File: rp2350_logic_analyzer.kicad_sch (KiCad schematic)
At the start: 35 parts, among them J1 Conn_02x04, J2 Conn_01x03, J3 Conn_01x03, J4 Conn_01x03, J5 Conn_01x03, U2 TLV3501AIDBV, U3 TLV3501AIDBV, U4 TLV3501AIDBV, U5 TLV3501AIDBV, U6 SRV05-4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

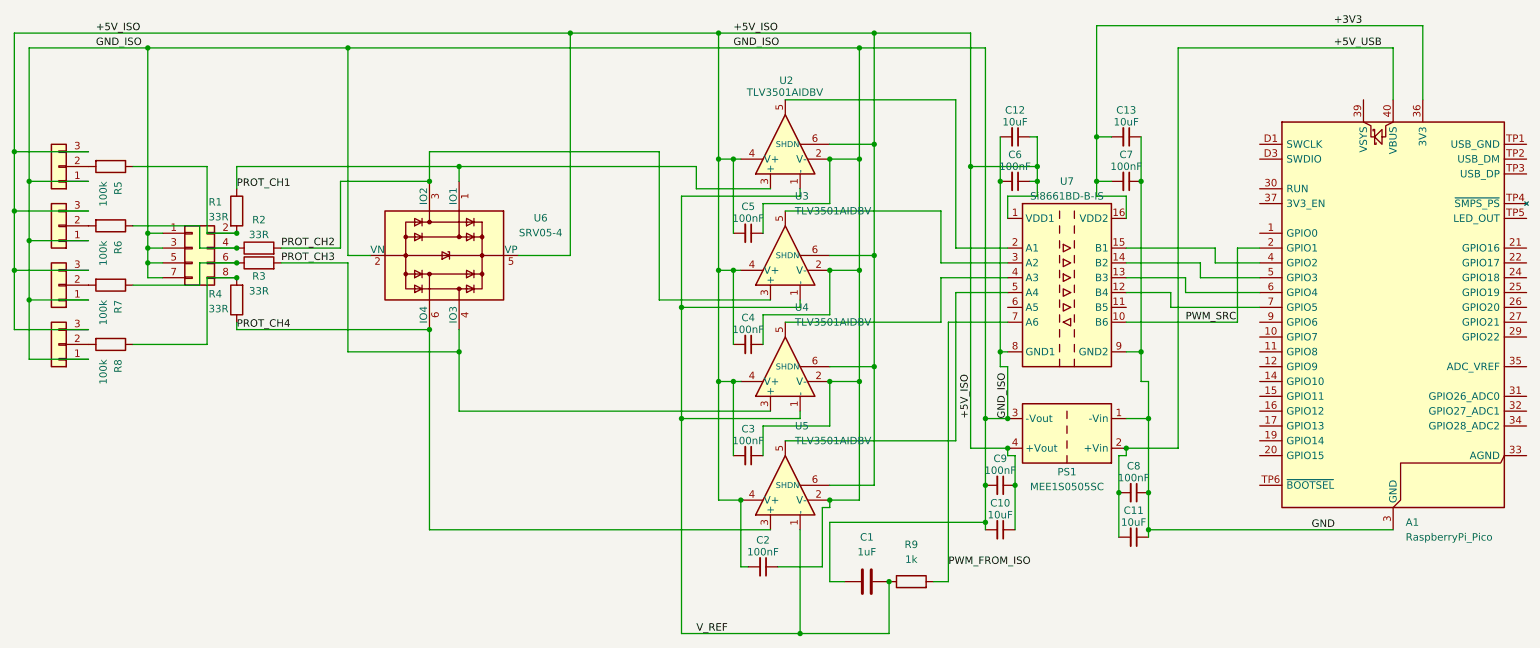
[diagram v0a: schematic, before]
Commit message: Revamp power supply side
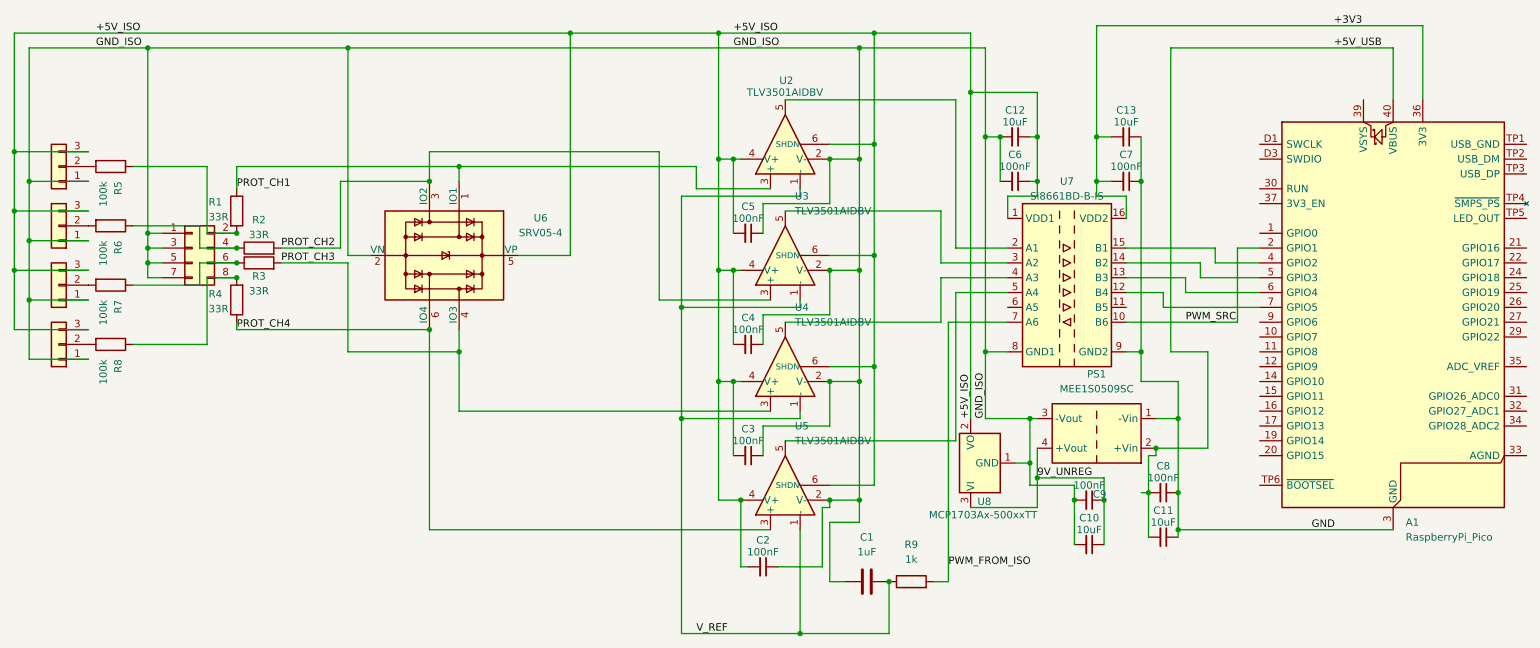
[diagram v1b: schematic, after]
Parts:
- removed PS1: MEE1S0505SC, Converter_DCDC:Converter_DCDC_Murata_MEE1SxxxxSC_THT, symbol Converter_DCDC:MEE1S0505SC
- added PS1: MEE1S0509SC, Converter_DCDC:Converter_DCDC_Murata_MEE1SxxxxSC_THT, symbol Converter_DCDC:MEE1S0509SC
- added U8: MCP1703Ax-500xxTT, Package_TO_SOT_SMD:SOT-23, symbol Regulator_Linear:MCP1703Ax-500xxTT
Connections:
- net +5V_ISO: now also U8.2 (VO); no longer C10.1, C9.1
- net +5V_USB: now also PS1.2 (+Vin)
- net GND: now also PS1.1 (-Vin)
- net GND_ISO: now also PS1.3 (-Vout), U8.1 (GND)
- new net 9V_UNREG: C10.1, C9.1, PS1.4 (+Vout), U8.3 (VI)
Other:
- moved on the sheet: C10, C11, C8, C9
